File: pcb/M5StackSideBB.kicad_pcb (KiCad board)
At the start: 2 copper layers, 100 x 50 mm, 15 parts, among them J1 Conn_01x14, J2 Conn_01x14, J3 Conn_02x15_Odd_Even, J4 Conn_02x15_Odd_Even

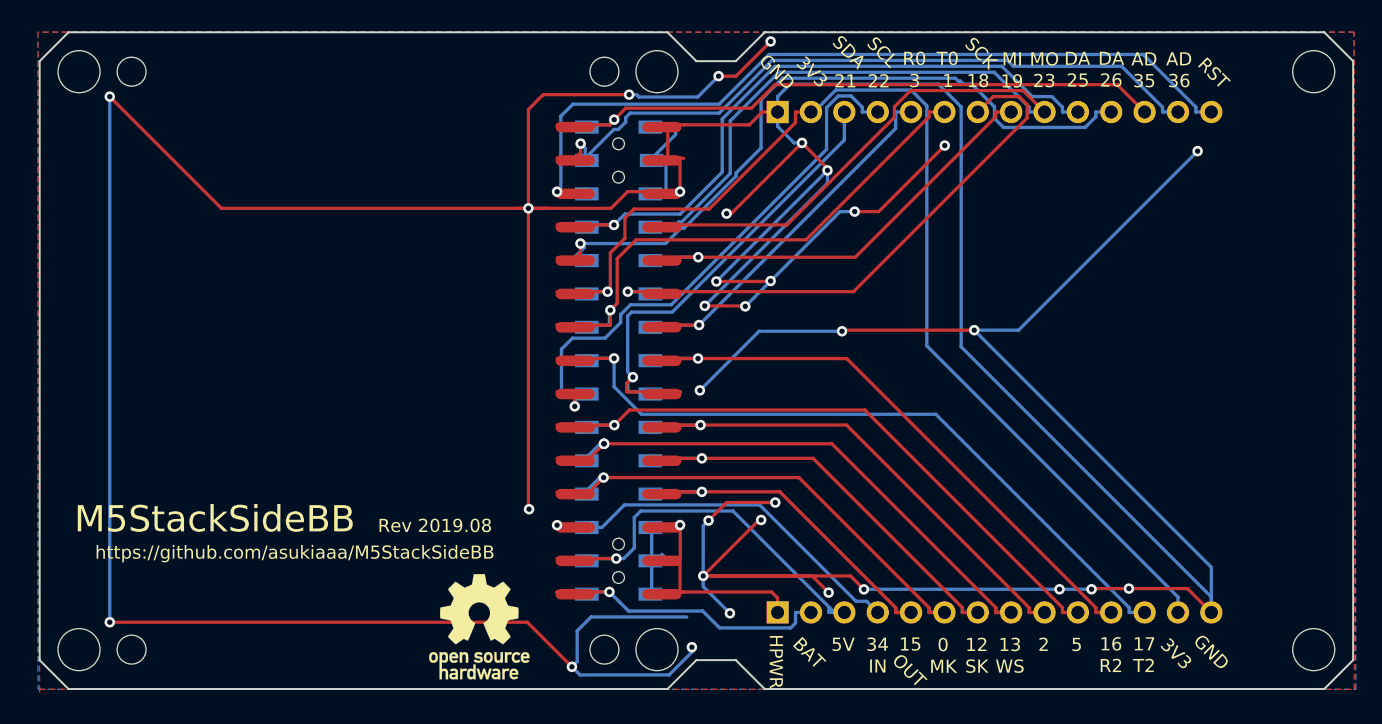
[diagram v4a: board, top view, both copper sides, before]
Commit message: Update spacer pad style
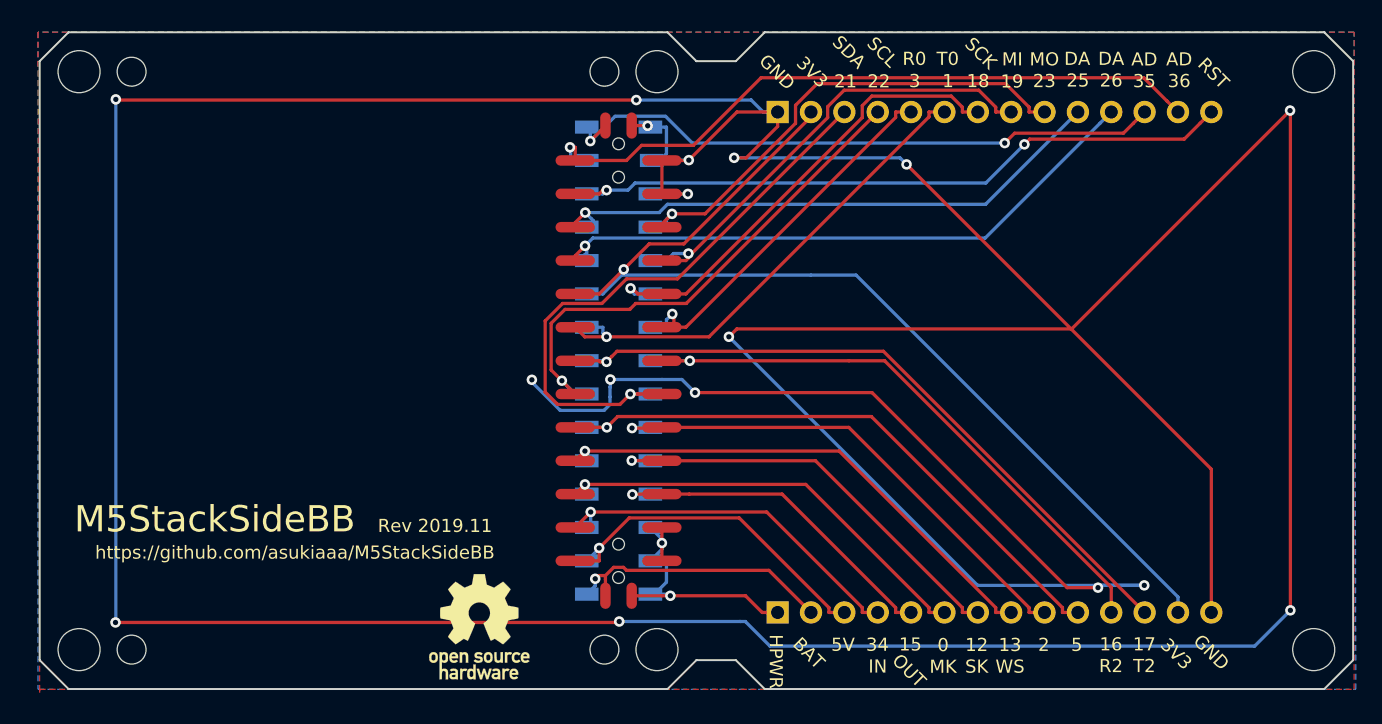
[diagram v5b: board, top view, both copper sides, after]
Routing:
- net GND: track 502.2 -> 454.9 mm, vias 33 -> 17
- net G23: track 71.7 -> 38.1 mm, vias 0 -> 1
- net RST: track 63.8 -> 52.6 mm, vias 1 -> 2
- net G21: track 37.5 -> 45.9 mm
- net G26: track 55.9 -> 48.2 mm
- net G18: track 43.2 -> 35.9 mm
- net G25: track 50.9 -> 44.0 mm
- net +3V3: track 87.0 -> 81.3 mm
- net +5V: track 31.8 -> 27.0 mm
- net G13: track 44.0 -> 39.6 mm, vias 2 -> 1
- net G0: track 37.8 -> 33.5 mm
- net G1: track 42.1 -> 37.8 mm
- net G22: track 43.7 -> 40.2 mm
- net G19: track 33.6 -> 36.7 mm
- net G17: track 56.4 -> 53.5 mm
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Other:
- board text added: "Rev 2019.11"
- board text removed: "Rev 2019.08"
